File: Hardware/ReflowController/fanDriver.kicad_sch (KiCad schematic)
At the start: 12 parts, among them U3 TB67H400AFNG

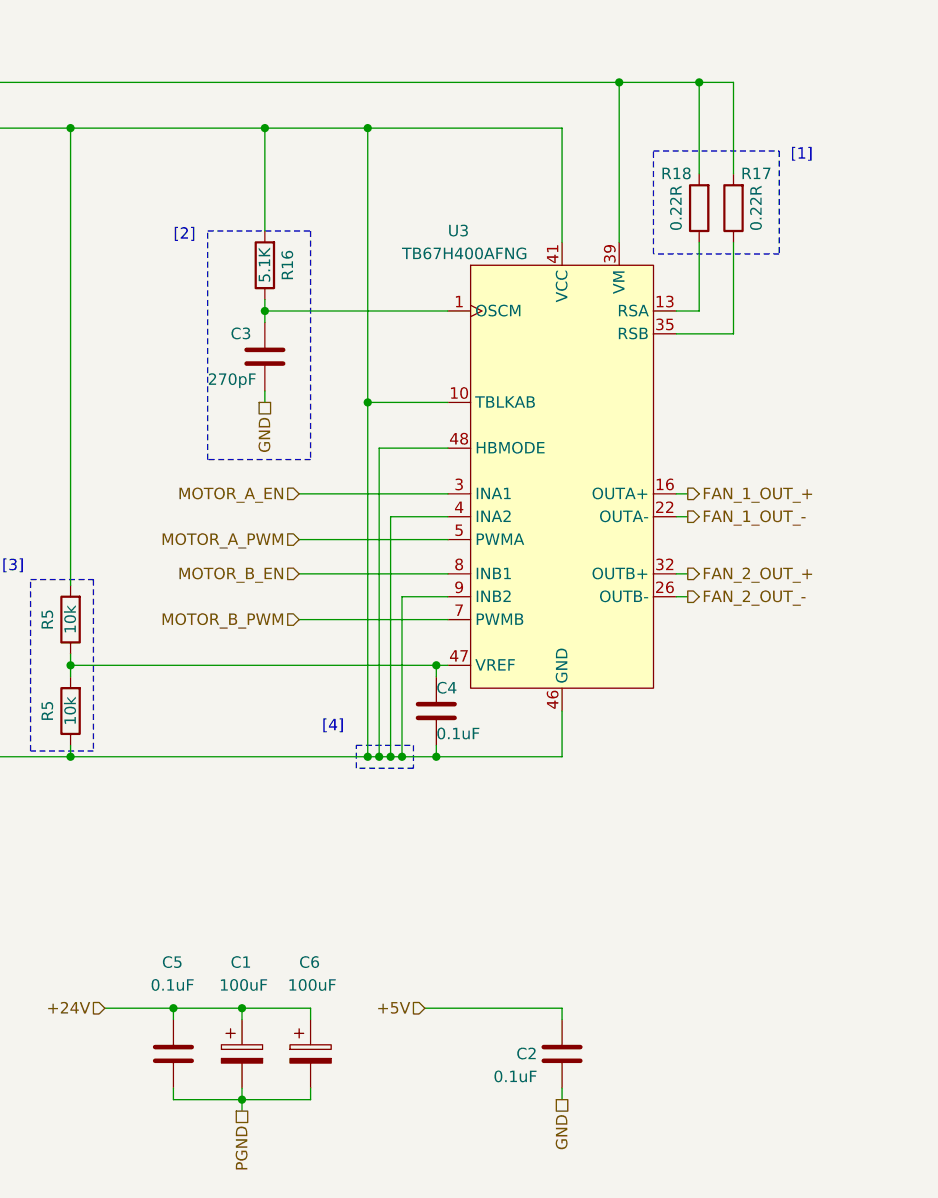
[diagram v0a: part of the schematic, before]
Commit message: finished the io control for the pcb, need to define what is the best way for a remote keypad
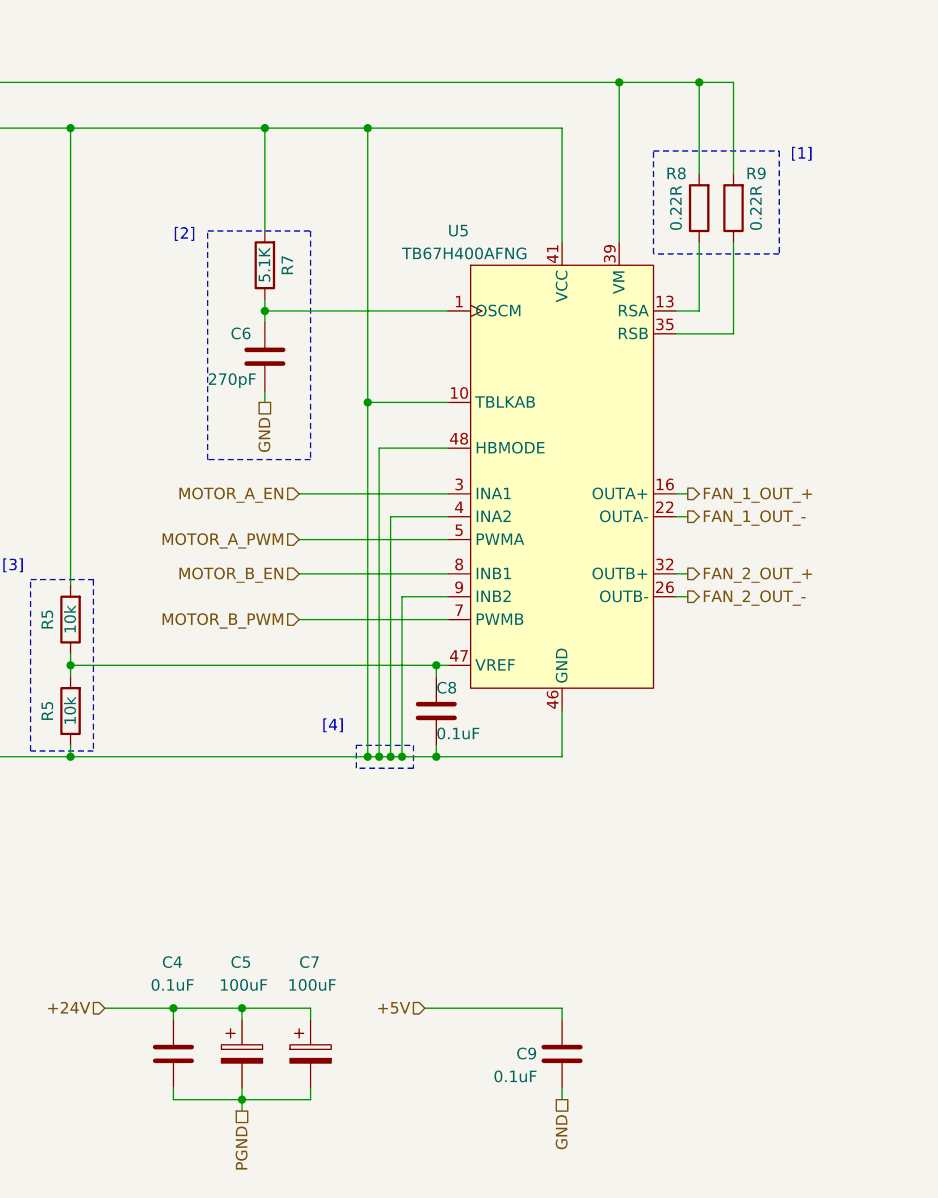
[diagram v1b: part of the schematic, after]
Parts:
- renumbered C5 to C4, C1 to C5, C3 to C6, C6 to C7, C4 to C8, C2 to C9, R16 to R7, R18 to R8, R17 to R9, U3 to U5
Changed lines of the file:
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@@
   (symbol (lib_id "350_power_driver_motor_dc:TB67H400AFNG,EL") (at 104.14 95.25 0) (unit 1)
     (in_bom yes) (on_board yes) (dnp no) (fields_autoplaced)
-    (property "Reference" "U3" (at 91.44 66.04 0)
+    (property "Reference" "U5" (at 91.44 66.04 0)
       (effects (font (size 1.27 1.27)) (justify left))
     )
@@
       (project "ReflowController"
         (path "/2394cc2a-b9b0-4c0b-be11-1fc6085b0d5c/88b069ca-209a-441b-9ebc-a973d3ca8ace"
-          (reference "U3") (unit 1)
+          (reference "U5") (unit 1)
         )
       )
@@
   (symbol (lib_id "Device:C_Polarized") (at 76.2 157.48 0) (unit 1)
     (in_bom yes) (on_board yes) (dnp no)
-    (property "Reference" "C6" (at 74.93 147.32 0)
+    (property "Reference" "C7" (at 74.93 147.32 0)
       (effects (font (size 1.27 1.27)) (justify left))
     )
@@
       (project "ReflowController"
         (path "/2394cc2a-b9b0-4c0b-be11-1fc6085b0d5c/88b069ca-209a-441b-9ebc-a973d3ca8ace"
-          (reference "C6") (unit 1)
+          (reference "C7") (unit 1)
         )
       )
@@
   (symbol (lib_id "Device:C") (at 104.14 157.48 0) (unit 1)
     (in_bom yes) (on_board yes) (dnp no)
-    (property "Reference" "C2" (at 99.06 157.48 0)
+    (property "Reference" "C9" (at 99.06 157.48 0)
       (effects (font (size 1.27 1.27)) (justify left))
     )
@@
       (project "ReflowController"
         (path "/2394cc2a-b9b0-4c0b-be11-1fc6085b0d5c/88b069ca-209a-441b-9ebc-a973d3ca8ace"
-          (reference "C2") (unit 1)
+          (reference "C9") (unit 1)
         )
       )
@@
         )
         (path "/2394cc2a-b9b0-4c0b-be11-1fc6085b0d5c/88b069ca-209a-441b-9ebc-a973d3ca8ace"
-          (reference "R20") (unit 1)
+          (reference "R5") (unit 1)
         )
       )
@@
   (symbol (lib_id "Device:C") (at 71.12 80.01 0) (unit 1)
     (in_bom yes) (on_board yes) (dnp no)
-    (property "Reference" "C3" (at 67.31 77.47 0)
+    (property "Reference" "C6" (at 67.31 77.47 0)
       (effects (font (size 1.27 1.27)) (justify left))
     )
@@
       (project "ReflowController"
         (path "/2394cc2a-b9b0-4c0b-be11-1fc6085b0d5c/88b069ca-209a-441b-9ebc-a973d3ca8ace"
-          (reference "C3") (unit 1)
+          (reference "C6") (unit 1)
         )
       )
@@
   (symbol (lib_id "Device:R") (at 119.38 63.5 180) (unit 1)
     (in_bom yes) (on_board yes) (dnp no)
-    (property "Reference" "R18" (at 116.84 59.69 0)
+    (property "Reference" "R8" (at 116.84 59.69 0)
       (effects (font (size 1.27 1.27)))
     )
@@
       (project "ReflowController"
         (path "/2394cc2a-b9b0-4c0b-be11-1fc6085b0d5c/88b069ca-209a-441b-9ebc-a973d3ca8ace"
-          (reference "R18") (unit 1)
+          (reference "R8") (unit 1)
         )
       )
@@
   (symbol (lib_id "Device:R") (at 71.12 69.85 180) (unit 1)
     (in_bom yes) (on_board yes) (dnp no)
-    (property "Reference" "R16" (at 73.66 69.85 90)
+    (property "Reference" "R7" (at 73.66 69.85 90)
       (effects (font (size 1.27 1.27)))
     )
@@
       (project "ReflowController"
         (path "/2394cc2a-b9b0-4c0b-be11-1fc6085b0d5c/88b069ca-209a-441b-9ebc-a973d3ca8ace"
-          (reference "R16") (unit 1)
+          (reference "R7") (unit 1)
         )
       )
@@
   (symbol (lib_id "Device:R") (at 123.19 63.5 180) (unit 1)
     (in_bom yes) (on_board yes) (dnp no)
-    (property "Reference" "R17" (at 125.73 59.69 0)
+    (property "Reference" "R9" (at 125.73 59.69 0)
       (effects (font (size 1.27 1.27)))
     )
@@
       (project "ReflowController"
         (path "/2394cc2a-b9b0-4c0b-be11-1fc6085b0d5c/88b069ca-209a-441b-9ebc-a973d3ca8ace"
-          (reference "R17") (unit 1)
+          (reference "R9") (unit 1)
         )
       )
@@
   (symbol (lib_id "Device:C_Polarized") (at 68.58 157.48 0) (unit 1)
     (in_bom yes) (on_board yes) (dnp no)
-    (property "Reference" "C1" (at 67.31 147.32 0)
+    (property "Reference" "C5" (at 67.31 147.32 0)
       (effects (font (size 1.27 1.27)) (justify left))
     )
@@
       (project "ReflowController"
         (path "/2394cc2a-b9b0-4c0b-be11-1fc6085b0d5c/88b069ca-209a-441b-9ebc-a973d3ca8ace"
-          (reference "C1") (unit 1)
+          (reference "C5") (unit 1)
         )
       )
@@
         )
         (path "/2394cc2a-b9b0-4c0b-be11-1fc6085b0d5c/88b069ca-209a-441b-9ebc-a973d3ca8ace"
-          (reference "R21") (unit 1)
+          (reference "R6") (unit 1)
         )
       )
@@
   (symbol (lib_id "Device:C") (at 60.96 157.48 0) (unit 1)
     (in_bom yes) (on_board yes) (dnp no)
-    (property "Reference" "C5" (at 59.69 147.32 0)
+    (property "Reference" "C4" (at 59.69 147.32 0)
       (effects (font (size 1.27 1.27)) (justify left))
     )
@@
       (project "ReflowController"
         (path "/2394cc2a-b9b0-4c0b-be11-1fc6085b0d5c/88b069ca-209a-441b-9ebc-a973d3ca8ace"
-          (reference "C5") (unit 1)
+          (reference "C4") (unit 1)
         )
       )
@@
   (symbol (lib_id "Device:C") (at 90.17 119.38 0) (unit 1)
     (in_bom yes) (on_board yes) (dnp no)
-    (property "Reference" "C4" (at 90.17 116.84 0)
+    (property "Reference" "C8" (at 90.17 116.84 0)
       (effects (font (size 1.27 1.27)) (justify left))
     )
@@
       (project "ReflowController"
         (path "/2394cc2a-b9b0-4c0b-be11-1fc6085b0d5c/88b069ca-209a-441b-9ebc-a973d3ca8ace"
-          (reference "C4") (unit 1)
-        )
-      )
+          (reference "C8") (unit 1)
+        )
+      )

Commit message: Wrking with edwin on the hwole schematic
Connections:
- net +5V: no longer C4.2, C5.2, C7.2, C8.2, R5.1, U5.10 (TBLKAB), U5.11 (GND), U5.20 (GND), U5.24 (GND), U5.25 (GND), U5.29 (GND), U5.4 (INA2), U5.46 (GND), U5.48 (HBMODE), U5.9 (INB2)
- net GND: now also C8.2, R5.1, U5.10 (TBLKAB), U5.4 (INA2), U5.48 (HBMODE), U5.9 (INB2)
- new net PGND: C4.2, C5.2, C7.2, U5.11 (GND), U5.20 (GND), U5.24 (GND), U5.25 (GND), U5.29 (GND), U5.46 (GND)
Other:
- note added: "[4] - INA2 & INB2 = L : Motors will alwas rotate Clockwise - Break option is removed : INx1 & INx2 != H - HBMODE = L : Opperatiom mode only supports dual motor - TBLKAB = L : noise rejection time = 400 ns + Foscm * 4 clk (DS : page 8 - 10 )"
- note removed: "[4] - INB1 & INB2 = L : Motors will alwas rotate Clockwise - Break option is removed : INx1 & INx2 != H - HBMODE = L : Opperatiom mode only supports dual motor - TBLKAB = L : noise rejection time = 400 ns + Foscm * 4 clk (DS : page 8 - 10 )"
- moved on the sheet: C4, C5, C6, C7, C8, C9, R5, R7, R8, R9, U5
